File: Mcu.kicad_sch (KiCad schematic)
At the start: 35 parts

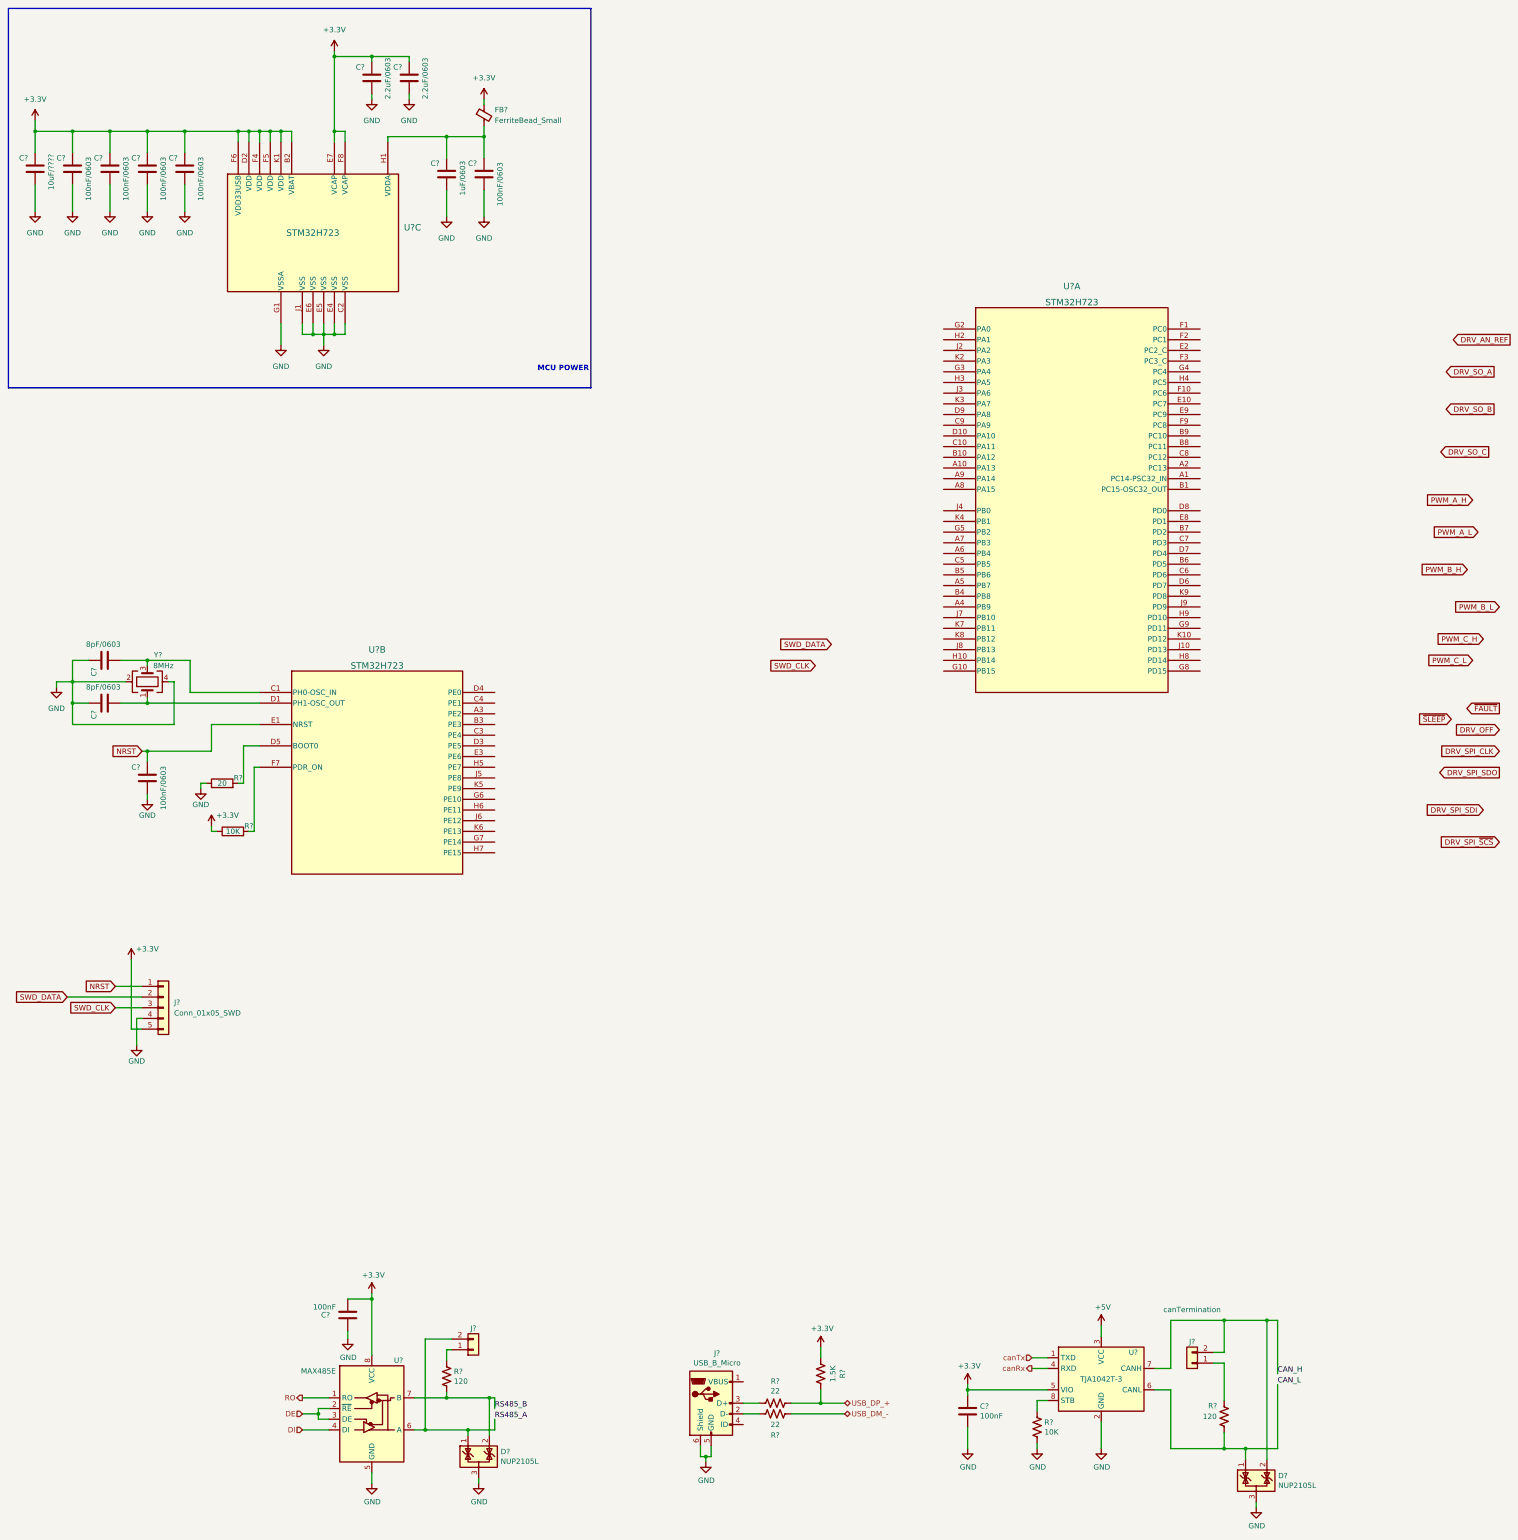
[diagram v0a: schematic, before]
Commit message: Add IO sub schematic, add communications
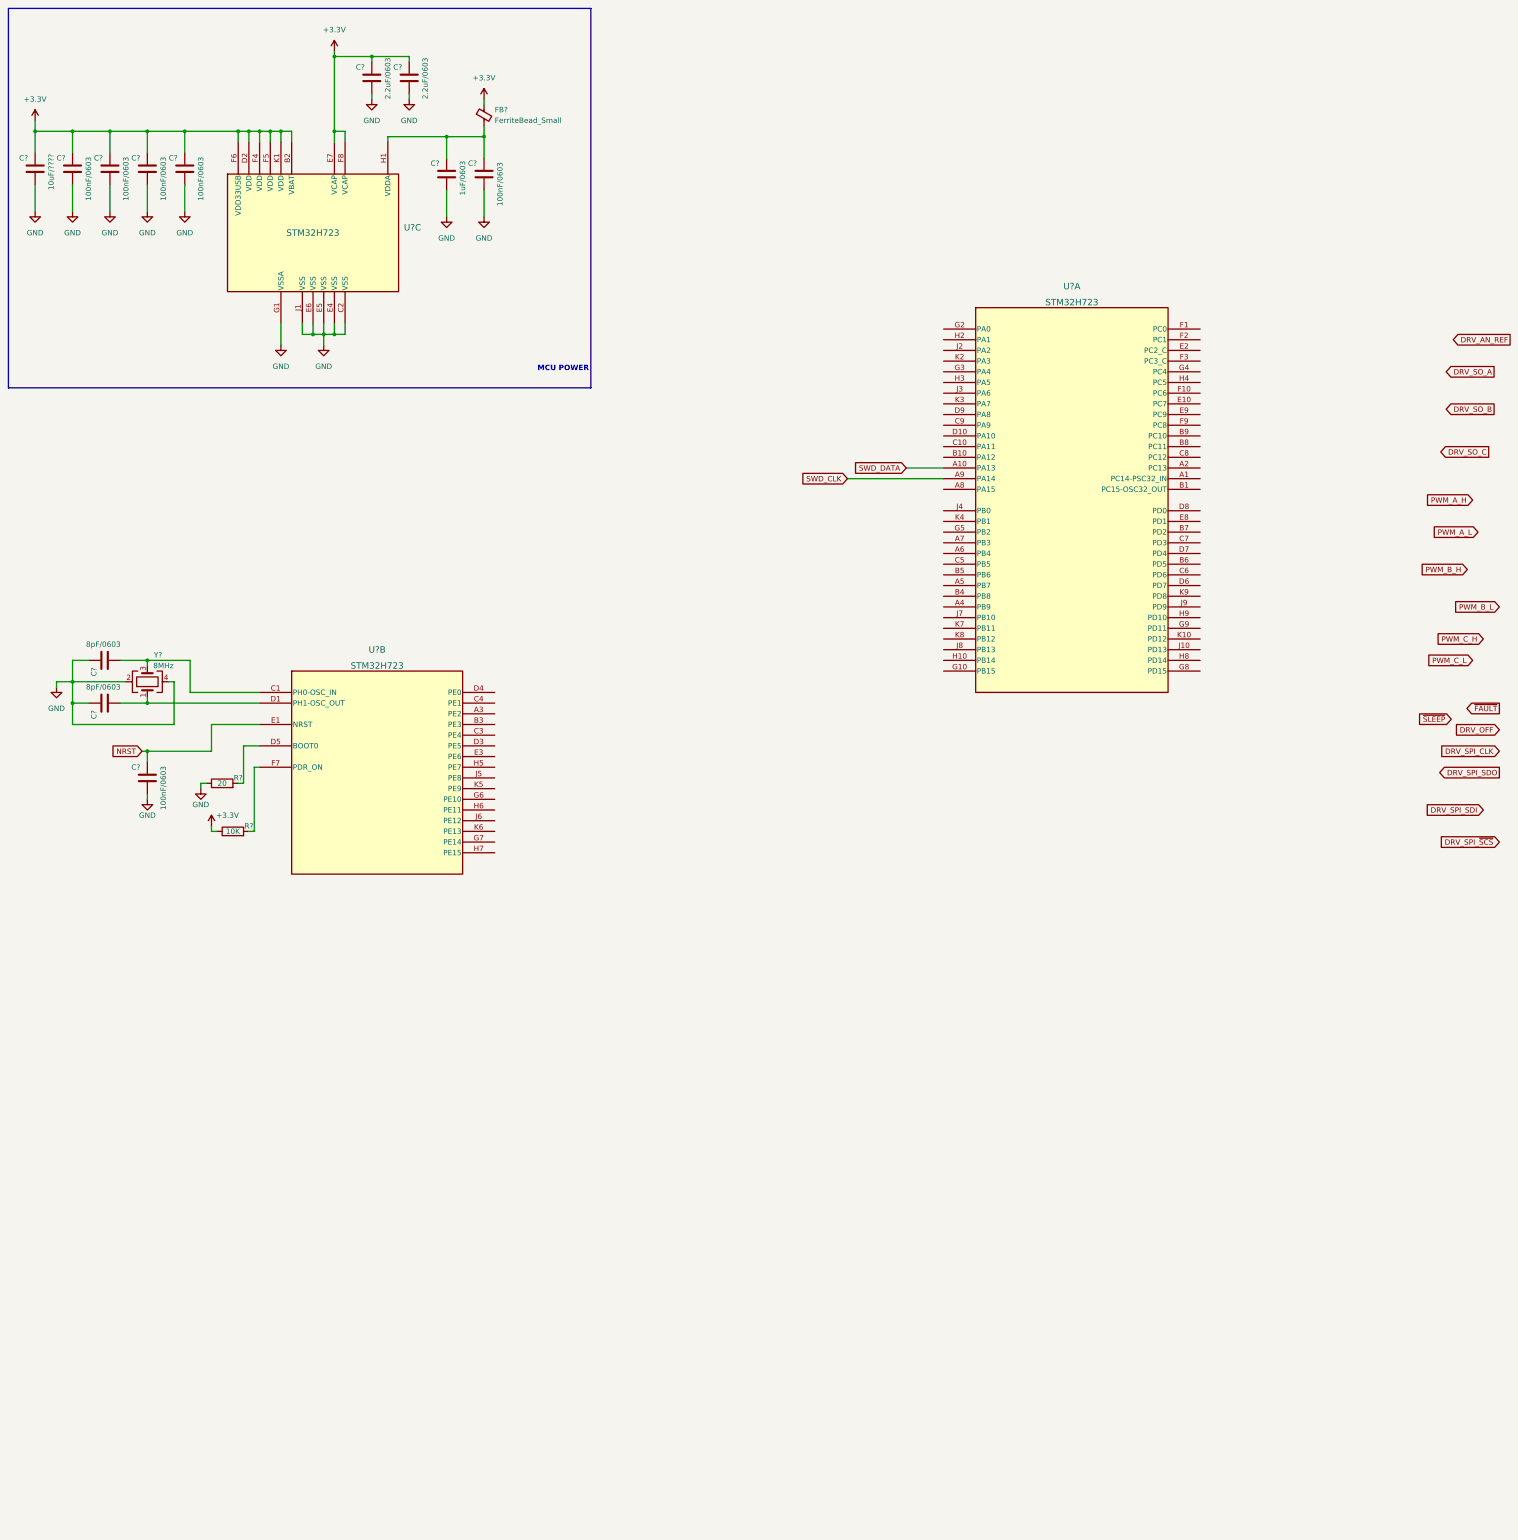
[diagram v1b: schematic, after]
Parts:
- removed C? (x2): 100nF, asemsys_footprint_lib:C_0402, symbol Device:C
- removed D? (x2): NUP2105L, asemsys_footprint_lib:SOT23-3, symbol Power_Protection:NUP2105L
- removed J?: canTermination, asemsys_footprint_lib:HEADER_1x2, symbol Connector_Generic:Conn_01x02
- removed J?: Conn_01x05_SWD, symbol Connector_Generic:Conn_01x05
- removed J?: ~, symbol Connector_Generic:Conn_01x02
- removed J?: USB_B_Micro, Connector_USB:USB_Micro-B_Molex-105017-0001, symbol allDrive-rescue:USB_B_Micro-Connector
- removed R? (x2): 120, asemsys_footprint_lib:R_0402, symbol Device:R_US
- removed R? (x2): 22, asemsys_footprint_lib:R_0402, symbol Device:R_US
- removed R?: 1.5K, asemsys_footprint_lib:R_0402, symbol Device:R_US
- removed R?: 10K, asemsys_footprint_lib:R_0402, symbol Device:R_US
- removed U?: TJA1042T-3, asemsys_footprint_lib:SOIC-8, symbol Interface_CAN_LIN:TJA1042T-3
- removed U?: MAX485E, asemsys_footprint_lib:SOIC-8, symbol Interface_UART:MAX485E
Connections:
- net SWD_CLK: now also U?.A9 (PA14)
- net SWD_DATA: now also U?.A10 (PA13)

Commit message: add IO, MCU, power sheets
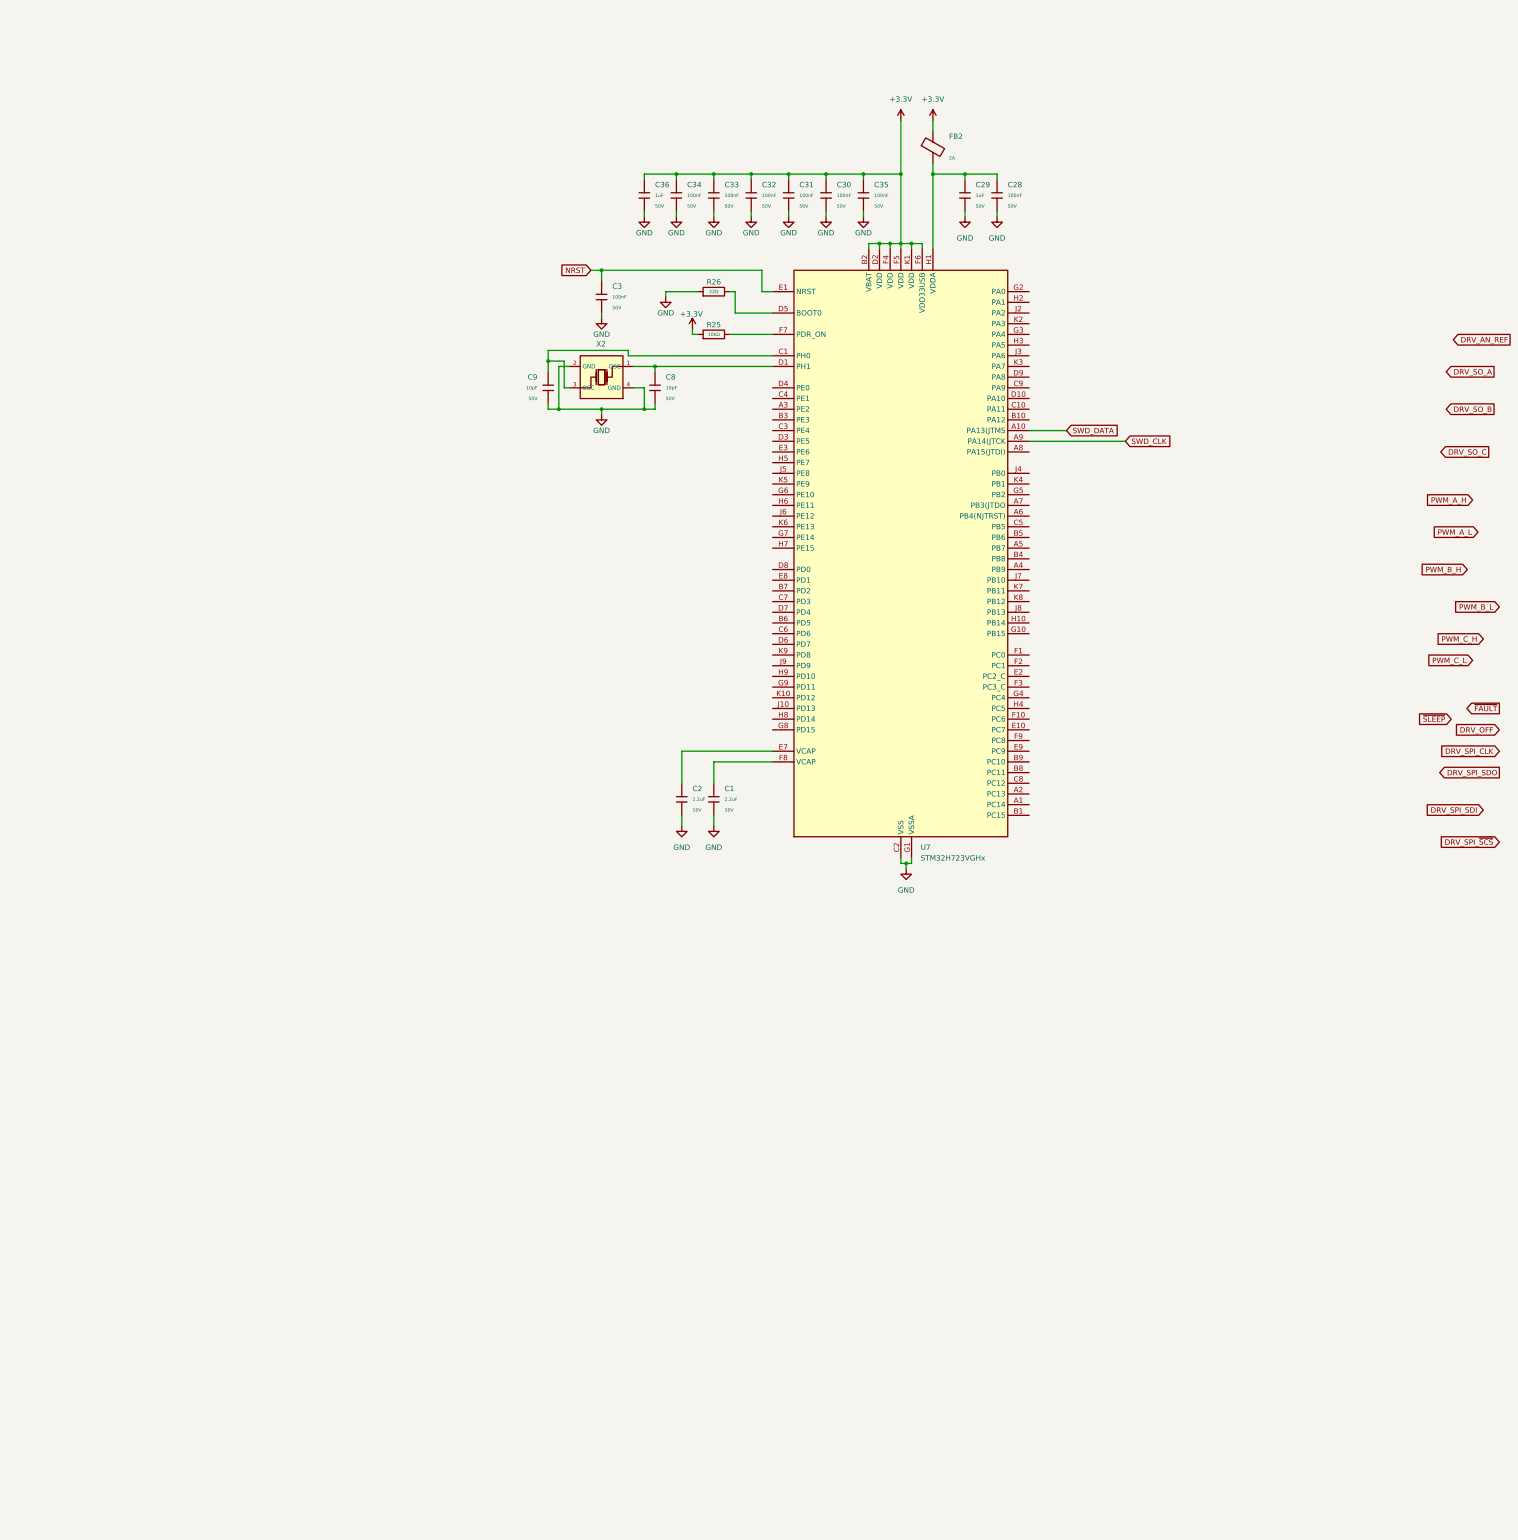
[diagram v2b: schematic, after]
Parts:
- removed C? (x6): 100nF/0603, Capacitor_SMD:C_0603_1608Metric, symbol Device:C
- removed C?: 10uF/????, Capacitor_SMD:C_0603_1608Metric, symbol Device:C
- removed C?: 1uF/0603, Capacitor_SMD:C_0603_1608Metric, symbol Device:C
- removed C? (x2): 8pF/0603, Capacitor_SMD:C_0603_1608Metric, symbol Device:C
- removed C? (x2): 2.2uF/0603, Capacitor_SMD:C_0603_1608Metric, symbol Device:C
- removed FB?: FerriteBead_Small, symbol Device:FerriteBead_Small
- removed R?: 20, Resistor_SMD:R_0603_1608Metric, symbol Device:R
- removed R?: 10K, Resistor_SMD:R_0603_1608Metric, symbol Device:R
- removed U? (x3): STM32H723, TFBGA100_STM, symbol STM32H723VGH6:STM32H723
- removed Y?: 8MHz, symbol Device:Crystal_GND24
- added C1, C2: 2.2uF, PCM_JLCPCB:C_0603, symbol PCM_JLCPCB-Capacitors:0603,2.2uF
- added C28, C3, C30, C31, C32, C33, C34, C35: 100nF, PCM_JLCPCB:C_0603, symbol PCM_JLCPCB-Capacitors:0603,100nF
- added C29, C36: 1uF, PCM_JLCPCB:C_0603, symbol PCM_JLCPCB-Capacitors:0603,1uF
- added C8, C9: 10pF, PCM_JLCPCB:C_0603, symbol PCM_JLCPCB-Capacitors:0603,10pF
- added FB2: ~, PCM_JLCPCB:FB_0603, symbol PCM_JLCPCB-Inductors:Ferrite,0603,(2)
- added R25: 10kΩ, PCM_JLCPCB:R_0603, symbol PCM_JLCPCB-Resistors:0603,10kΩ
- added R26: 22Ω, PCM_JLCPCB:R_0603, symbol PCM_JLCPCB-Resistors:0603,22Ω
- added U7: STM32H723VGHx, Package_BGA:TFBGA-100_8x8mm_Layout10x10_P0.8mm, symbol MCU_ST_STM32H7:STM32H723VGHx
- added X2: X322516MLB4SI, PCM_JLCPCB:OSC-SMD_4P-L3.2-W2.5-BL, symbol PCM_JLCPCB-Crystals:Crystal, 16MHz, 9pF
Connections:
- net +3.3V: now also C30.1, C31.1, C32.1, C33.1, C34.1, C35.1, C36.1, FB2.1, R25.1, U7.B2 (VBAT), U7.D2 (VDD), U7.F4 (VDD), U7.F5 (VDD), U7.F6 (VDD33USB), U7.K1 (VDD)
- net GND: now also C1.2, C2.2, C28.2, C29.2, C3.2, C30.2, C31.2, C32.2, C33.2, C34.2, C35.2, C36.2, C8.2, C9.2, R26.1, U7.C2 (VSS), U7.E4 (VSS), U7.E5 (VSS), U7.E6 (VSS), U7.G1 (VSSA), U7.J1 (VSS), X2.2 (GND), X2.4 (GND)
- net NRST: now also C3.1, U7.E1 (NRST)
- net SWD_CLK: now also U7.A9 (PA14(JTCK)
- net SWD_DATA: now also U7.A10 (PA13(JTMS)
- new net: C8.1, U7.D1 (PH1), X2.1 (OSC)
- new net: C9.1, U7.C1 (PH0), X2.3 (OSC)
- new net: R26.2, U7.D5 (BOOT0)
- new net: C2.1, U7.E7 (VCAP)
- new net: C28.1, C29.1, FB2.2, U7.H1 (VDDA)
- new net: R25.2, U7.F7 (PDR_ON)
- new net: C1.1, U7.F8 (VCAP)
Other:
- note removed: "MCU POWER"
